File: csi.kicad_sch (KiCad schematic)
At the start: 36 parts, among them J6 WE_68715014522, J7 WE_68715014022, U4 PCA9547BS,118

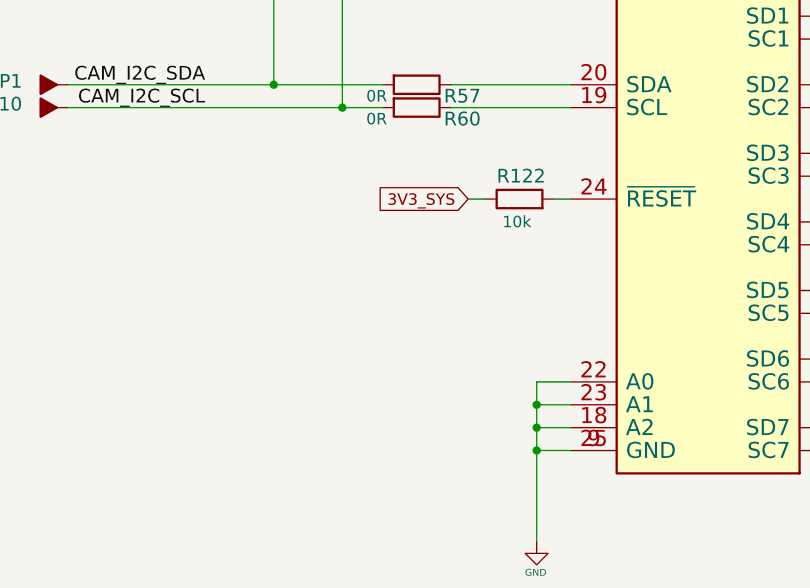
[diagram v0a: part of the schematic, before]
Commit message: Added possibility to reset I2C mux from SoM GPIO
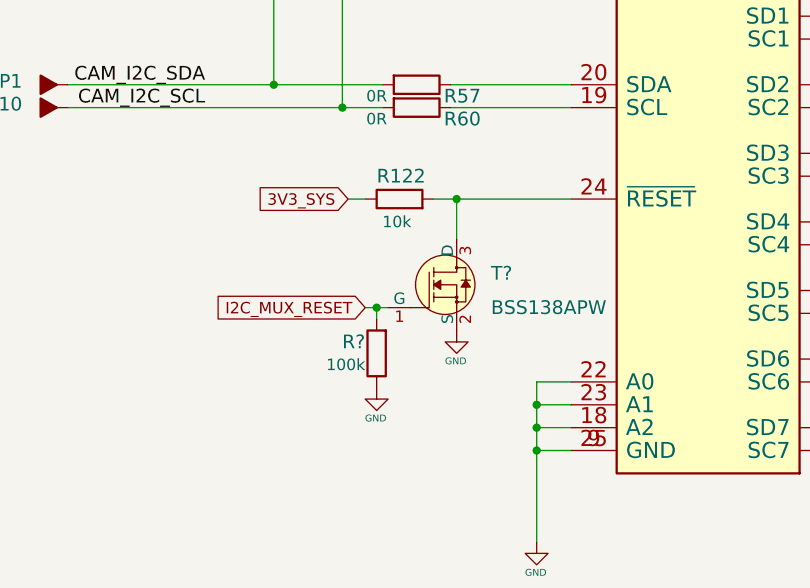
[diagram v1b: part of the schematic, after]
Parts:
- added R?: R_100k_0402, jetson-nano-baseboard-footprints:0402-res, symbol jetson-nano-baseboard:R_100k_0402
- added T?: BSS138APW, jetson-nano-baseboard-footprints:SC70-3, symbol jetson-nano-baseboard:BSS138APW
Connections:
- net GND: now also R?.1, T?.2 (S)
- net at R122.2, U4.24 (~{RESET}): now also T?.3 (D)
- new net I2C_MUX_RESET: R?.2, T?.1 (G)
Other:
- moved on the sheet: R122
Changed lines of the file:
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@@
   (junction (at 272.415 124.46) (diameter 0) (color 0 0 0 0)
   )
+  (junction (at 177.8 248.92) (diameter 0) (color 0 0 0 0)
+  )
   (junction (at 262.255 124.46) (diameter 0) (color 0 0 0 0)
   )
@@
   (junction (at 201.93 106.045) (diameter 0) (color 0 0 0 0)
   )
+  (junction (at 186.69 236.855) (diameter 0) (color 0 0 0 0)
+  )
   (junction (at 195.58 262.255) (diameter 0) (color 0 0 0 0)
   )
@@
     (stroke (width 0) (type default) (color 0 0 0 0))
   )
+  (wire (pts (xy 176.53 248.92) (xy 177.8 248.92))
+    (stroke (width 0) (type default) (color 0 0 0 0))
+  )
   (wire (pts (xy 166.37 198.755) (xy 173.99 198.755))
     (stroke (width 0) (type default) (color 0 0 0 0))
@@
     (stroke (width 0) (type default) (color 0 0 0 0))
   )
-  (wire (pts (xy 187.96 236.855) (xy 189.865 236.855))
+  (wire (pts (xy 174.625 236.855) (xy 176.53 236.855))
     (stroke (width 0) (type default) (color 0 0 0 0))
   )
@@
     (stroke (width 0) (type default) (color 0 0 0 0))
   )
-  (wire (pts (xy 197.485 236.855) (xy 199.39 236.855))
+  (wire (pts (xy 184.15 236.855) (xy 186.69 236.855))
     (stroke (width 0) (type default) (color 0 0 0 0))
   )
@@
     (stroke (width 0) (type default) (color 0 0 0 0))
   )
+  (wire (pts (xy 186.69 236.855) (xy 186.69 241.3))
+    (stroke (width 0) (type default) (color 0 0 0 0))
+  )
   (wire (pts (xy 280.035 52.705) (xy 300.99 52.705))
     (stroke (width 0) (type default) (color 0 0 0 0))
@@
     (stroke (width 0) (type default) (color 0 0 0 0))
   )
+  (wire (pts (xy 186.69 236.855) (xy 199.39 236.855))
+    (stroke (width 0) (type default) (color 0 0 0 0))
+  )
   (wire (pts (xy 272.415 123.19) (xy 272.415 124.46))
     (stroke (width 0) (type default) (color 0 0 0 0))
@@
     (stroke (width 0) (type default) (color 0 0 0 0))
   )
+  (wire (pts (xy 177.8 250.19) (xy 177.8 248.92))
+    (stroke (width 0) (type default) (color 0 0 0 0))
+  )
   (wire (pts (xy 201.93 106.045) (xy 201.93 113.665))
     (stroke (width 0) (type default) (color 0 0 0 0))
@@
     (stroke (width 0) (type default) (color 0 0 0 0))
   )
+  (wire (pts (xy 177.8 248.92) (xy 179.07 248.92))
+    (stroke (width 0) (type default) (color 0 0 0 0))
+  )
   (image (at 38.1 271.6022) (scale 0.4)
     (data
@@
     )
   )
-  (global_label "3V3_SYS" (shape input) (at 187.96 236.855 180) (fields_autoplaced)
+  (global_label "3V3_SYS" (shape input) (at 174.625 236.855 180) (fields_autoplaced)
     (effects (font (size 1.27 1.27)) (justify right))
-    (property "Intersheet References" "${INTERSHEET_REFS}" (id 0) (at 0 0 0)
+    (property "Intersheet References" "${INTERSHEET_REFS}" (id 0) (at -13.335 0 0)
       (effects (font (size 1.27 1.27)) hide)
     )
@@
     )
   )
+  (global_label "I2C_MUX_RESET" (shape input) (at 176.53 248.92 180) (fields_autoplaced)
+    (effects (font (size 1.27 1.27)) (justify right))
+    (property "Intersheet References" "${INTERSHEET_REFS}" (id 0) (at 159.4496 248.8406 0)
+      (effects (font (size 1.27 1.27)) (justify right) hide)
+    )
+  )
   (global_label "3V3_SYS" (shape input) (at 196.85 194.945 90) (fields_autoplaced)
     (effects (font (size 1.27 1.27)) (justify left))
@@
     (pin "25")
   )
-  (symbol (lib_id "jetson-nano-baseboard:R_10k_0402") (at 193.675 236.855 0) (unit 1)
+  (symbol (lib_id "jetson-nano-baseboard:R_10k_0402") (at 180.34 236.855 0) (unit 1)
     (in_bom yes) (on_board yes)
-    (property "Reference" "R122" (id 0) (at 191.135 234.315 0)
+    (property "Reference" "R122" (id 0) (at 177.8 234.315 0)
       (effects (font (size 1.524 1.524)) (justify left))
     )
-    (property "Value" "R_10k_0402" (id 1) (at 193.675 240.665 0)
+    (property "Value" "R_10k_0402" (id 1) (at 180.34 240.665 0)
       (effects (font (size 1.524 1.524)) hide)
     )
-    (property "Footprint" "jetson-nano-baseboard-footprints:0402-res" (id 2) (at 198.755 231.775 0)
+    (property "Footprint" "jetson-nano-baseboard-footprints:0402-res" (id 2) (at 185.42 231.775 0)
       (effects (font (size 1.524 1.524)) (justify left) hide)
     )
-    (property "Datasheet" "" (id 3) (at 193.675 236.855 0)
+    (property "Datasheet" "" (id 3) (at 180.34 236.855 0)
       (effects (font (size 1.27 1.27)) hide)
     )
-    (property "Manufacturer" "VISHAY" (id 4) (at 198.755 226.695 0)
+    (property "Manufacturer" "VISHAY" (id 4) (at 185.42 226.695 0)
       (effects (font (size 1.524 1.524)) (justify left) hide)
     )
-    (property "MPN" "CRCW040210K0FKEDHP" (id 5) (at 198.755 229.235 0)
+    (property "MPN" "CRCW040210K0FKEDHP" (id 5) (at 185.42 229.235 0)
       (effects (font (size 1.524 1.524)) (justify left) hide)
     )
-    (property "Val" "10k" (id 6) (at 191.77 239.395 0)
+    (property "Val" "10k" (id 6) (at 178.435 239.395 0)
       (effects (font (size 1.27 1.27)) (justify left))
     )
@@
     (pin "1")
   )
+  (symbol (lib_id "jetson-nano-baseboard:R_100k_0402") (at 177.8 254 90) (unit 1)
+    (in_bom yes) (on_board yes)
+    (property "Reference" "R?" (id 0) (at 176.53 252.73 90)
+      (effects (font (size 1.524 1.524)) (justify left))
+    )
+    (property "Value" "R_100k_0402" (id 1) (at 181.61 254 0)
+      (effects (font (size 1.524 1.524)) hide)
+    )
+    (property "Footprint" "jetson-nano-baseboard-footprints:0402-res" (id 2) (at 172.72 248.92 0)
+      (effects (font (size 1.524 1.524)) (justify left) hide)
+    )
+    (property "Datasheet" "" (id 3) (at 177.8 254 0)
+      (effects (font (size 1.27 1.27)) hide)
+    )
+    (property "Manufacturer" "VISHAY" (id 4) (at 167.64 248.92 0)
+      (effects (font (size 1.524 1.524)) (justify left) hide)
+    )
+    (property "MPN" "CRCW0402100KFKEDHP" (id 5) (at 170.18 248.92 0)
+      (effects (font (size 1.524 1.524)) (justify left) hide)
+    )
+    (property "Val" "100k" (id 6) (at 176.53 255.27 90)
+      (effects (font (size 1.27 1.27)) (justify left))
+    )
+    (pin "1")
+    (pin "2")
+  )
+  (symbol (lib_id "jetson-nano-baseboard:GND") (at 177.8 257.81 0) (unit 1)
+    (in_bom yes) (on_board yes)
+    (property "Reference" "#GND?" (id 0) (at 177.8 257.81 0)
+      (effects (font (size 0.508 0.508)) hide)
+    )
+    (property "Value" "GND" (id 1) (at 177.6984 261.2136 0)
+      (effects (font (size 0.762 0.762)))
+    )
+    (property "Footprint" "" (id 2) (at 177.8 257.81 0)
+      (effects (font (size 1.778 1.778)) hide)
+    )
+    (property "Datasheet" "" (id 3) (at 177.8 257.81 0)
+      (effects (font (size 1.778 1.778)) hide)
+    )
+    (pin "1")
+  )
+  (symbol (lib_id "jetson-nano-baseboard:GND") (at 186.69 251.46 0) (unit 1)
+    (in_bom yes) (on_board yes)
+    (property "Reference" "#GND?" (id 0) (at 186.69 251.46 0)
+      (effects (font (size 0.508 0.508)) hide)
+    )
+    (property "Value" "GND" (id 1) (at 186.5884 254.8636 0)
+      (effects (font (size 0.762 0.762)))
+    )
+    (property "Footprint" "" (id 2) (at 186.69 251.46 0)
+      (effects (font (size 1.778 1.778)) hide)
+    )
+    (property "Datasheet" "" (id 3) (at 186.69 251.46 0)
+      (effects (font (size 1.778 1.778)) hide)
+    )
+    (pin "1")
+  )
+  (symbol (lib_id "jetson-nano-baseboard:BSS138APW") (at 186.69 246.38 0) (unit 1)
+    (in_bom yes) (on_board yes) (fields_autoplaced)
+    (property "Reference" "T?" (id 0) (at 190.5 245.11 0)
+      (effects (font (size 1.524 1.524)) (justify left))
+    )
+    (property "Value" "BSS138APW" (id 1) (at 190.5 248.92 0)
+      (effects (font (size 1.524 1.524)) (justify left))
+    )
+    (property "Footprint" "jetson-nano-baseboard-footprints:SC70-3" (id 2) (at 191.77 241.3 0)
+      (effects (font (size 1.524 1.524)) (justify left) hide)
+    )
+    (property "Datasheet" "" (id 3) (at 191.77 238.76 0)
+      (effects (font (size 1.524 1.524)) (justify left) hide)
+    )
+    (property "MPN" "BSS138PW" (id 4) (at 191.77 233.68 0)
+      (effects (font (size 1.524 1.524)) (justify left) hide)
+    )
+    (property "Manufacturer" "ON Semiconductor" (id 5) (at 191.77 218.44 0)
+      (effects (font (size 1.524 1.524)) (justify left) hide)
+    )
+    (pin "1")
+    (pin "2")
+    (pin "3")
+  )
 )

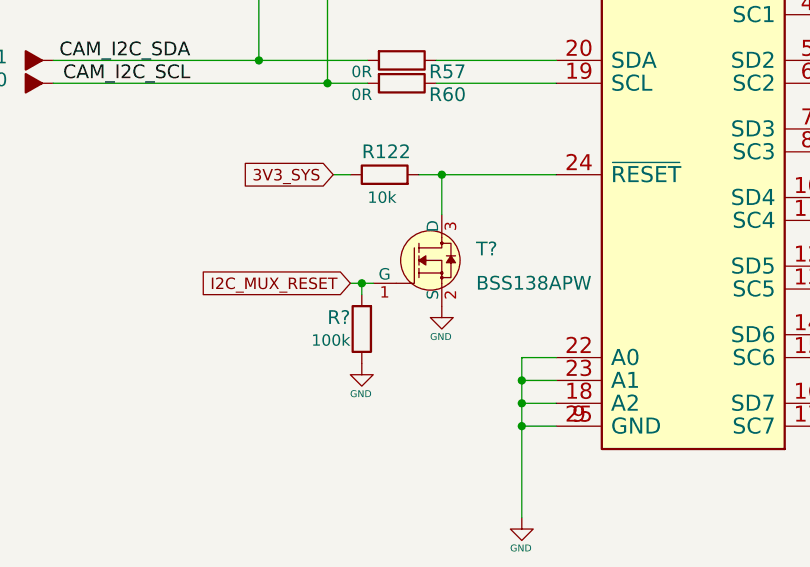
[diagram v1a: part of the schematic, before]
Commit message: Resolve TOOD on USB sheet
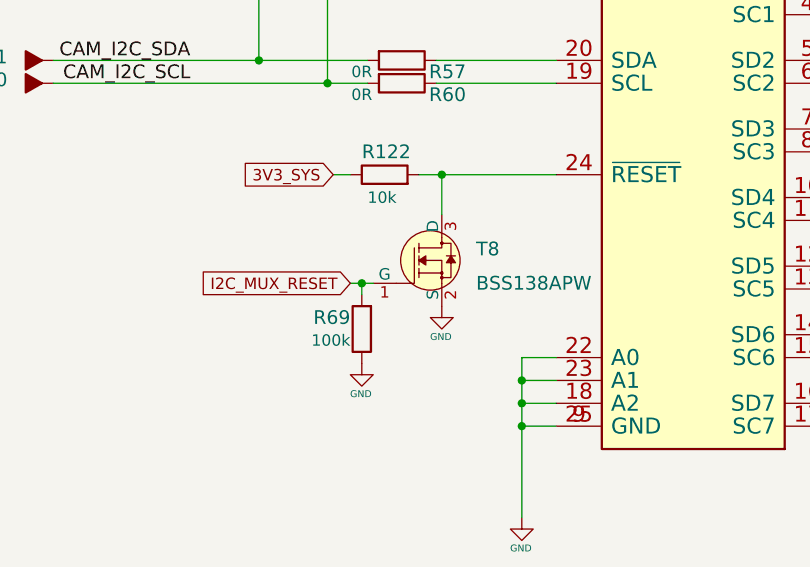
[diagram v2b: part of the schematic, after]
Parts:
- gave numbers to parts that had none: 2
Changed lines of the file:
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@@
   (symbol (lib_id "jetson-nano-baseboard:R_100k_0402") (at 177.8 254 90) (unit 1)
     (in_bom yes) (on_board yes)
-    (property "Reference" "R?" (id 0) (at 176.53 252.73 90)
+    (property "Reference" "R69" (id 0) (at 176.53 252.73 90)
       (effects (font (size 1.524 1.524)) (justify left))
     )
@@
   (symbol (lib_id "jetson-nano-baseboard:GND") (at 177.8 257.81 0) (unit 1)
     (in_bom yes) (on_board yes)
-    (property "Reference" "#GND?" (id 0) (at 177.8 257.81 0)
+    (property "Reference" "#GND0102" (id 0) (at 177.8 257.81 0)
       (effects (font (size 0.508 0.508)) hide)
     )
@@
   (symbol (lib_id "jetson-nano-baseboard:GND") (at 186.69 251.46 0) (unit 1)
     (in_bom yes) (on_board yes)
-    (property "Reference" "#GND?" (id 0) (at 186.69 251.46 0)
+    (property "Reference" "#GND0103" (id 0) (at 186.69 251.46 0)
       (effects (font (size 0.508 0.508)) hide)
     )
@@
   (symbol (lib_id "jetson-nano-baseboard:BSS138APW") (at 186.69 246.38 0) (unit 1)
     (in_bom yes) (on_board yes) (fields_autoplaced)
-    (property "Reference" "T?" (id 0) (at 190.5 245.11 0)
+    (property "Reference" "T8" (id 0) (at 190.5 245.11 0)
       (effects (font (size 1.524 1.524)) (justify left))
     )
